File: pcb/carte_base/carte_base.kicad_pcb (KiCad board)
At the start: 2 copper layers, 96 x 53 mm, 40 parts, among them J1 Conn_01x04, J2 Conn_01x02, J3 Conn_01x02, J4 Conn_01x02, SW1 FSMRA3JH04, U1 STM32L031, U2 DAC7563T, U3 TS9222IDT

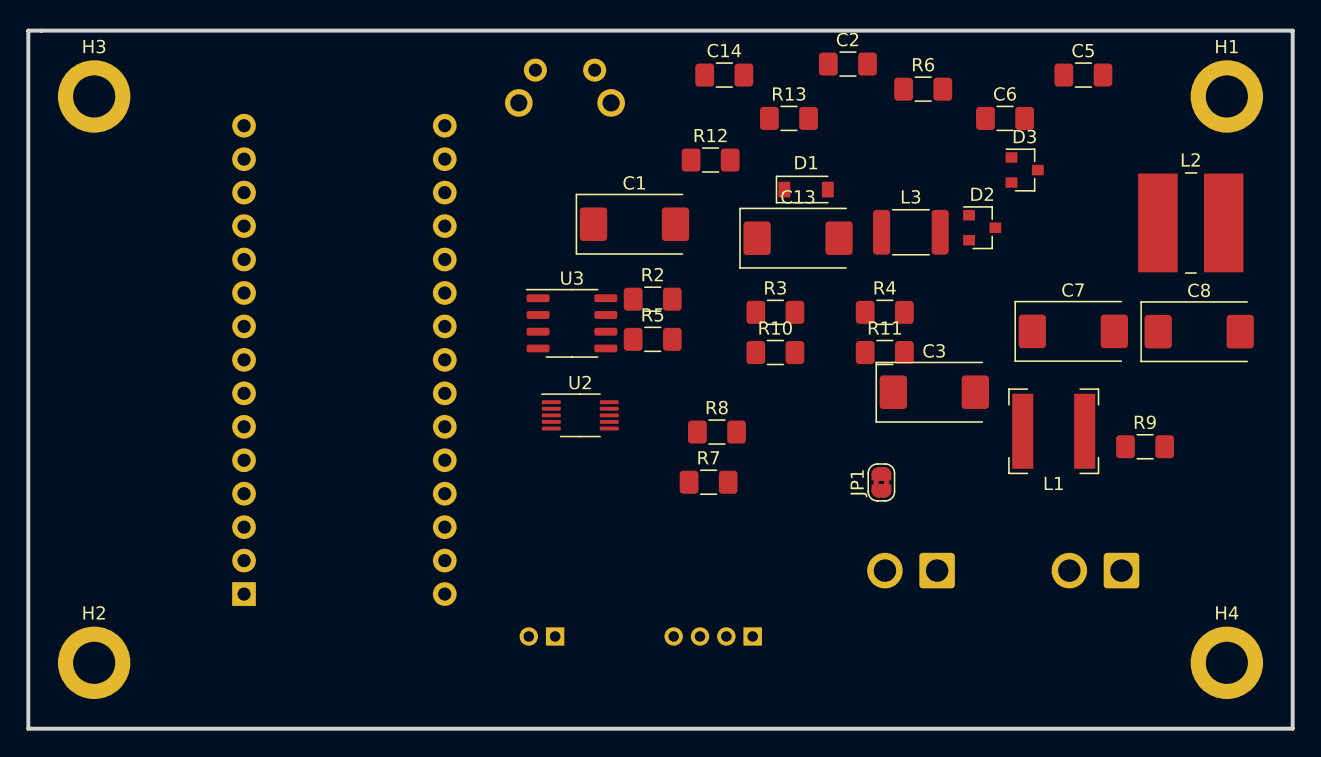
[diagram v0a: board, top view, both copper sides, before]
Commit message: Carte base finie
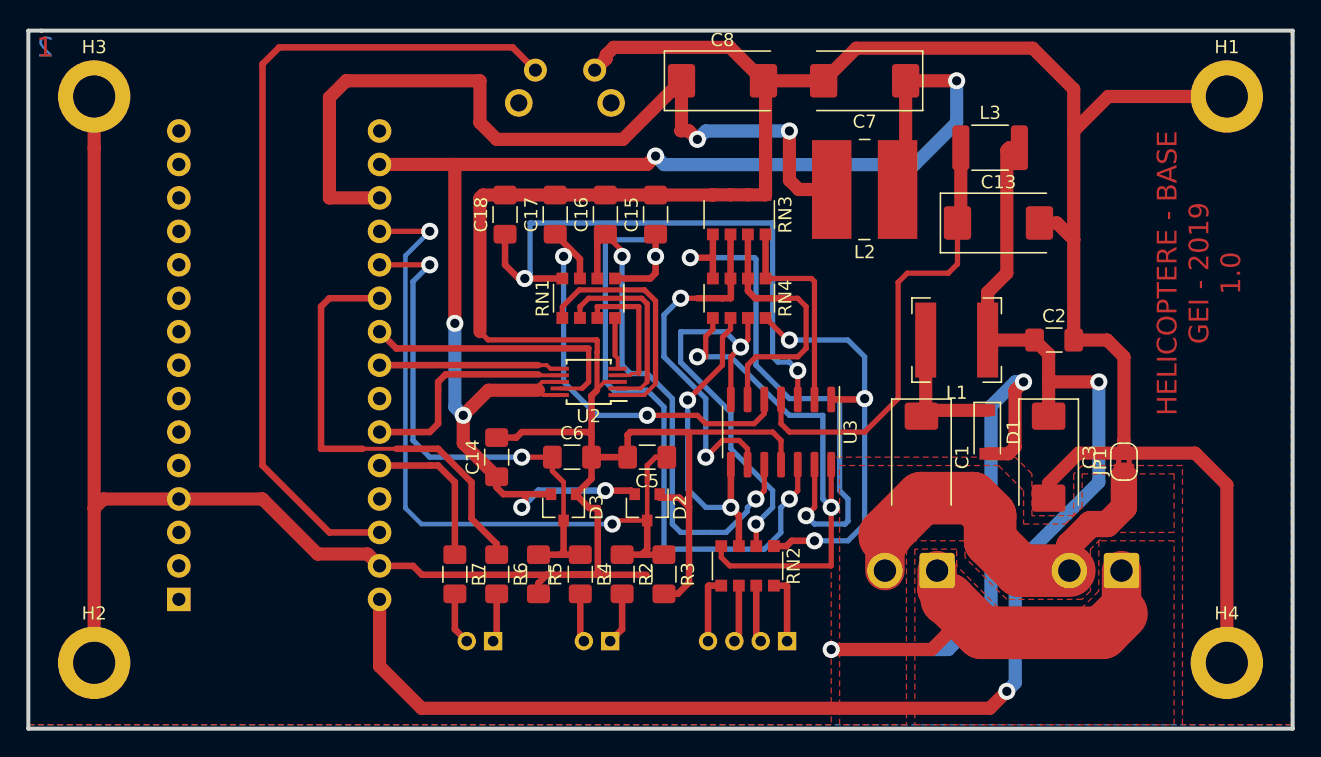
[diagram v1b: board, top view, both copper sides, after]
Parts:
- removed R10, R11, R12, R13, R8, R9: 1K, Resistor_SMD:R_1206_3216Metric_Pad1.42x1.75mm_HandSolder
- added C15: 22nF, Capacitor_SMD:C_1206_3216Metric_Pad1.42x1.75mm_HandSolder, F.Cu at (127.6, 74.0)
- added C16: 22nF, Capacitor_SMD:C_1206_3216Metric_Pad1.42x1.75mm_HandSolder, F.Cu at (123.8, 74.0)
- added C17: 22nF, Capacitor_SMD:C_1206_3216Metric_Pad1.42x1.75mm_HandSolder, F.Cu at (120.0, 74.0)
- added C18: 22nF, Capacitor_SMD:C_1206_3216Metric_Pad1.42x1.75mm_HandSolder, F.Cu at (116.2, 74.0)
- added J5: Conn_01x02, Insa:DF3A-2P-2DS, B.Cu at (123.2, 106.4)
- added RN1: 1K, Resistor_SMD:R_Array_Convex_4x1206, F.Cu at (122.5, 80.3)
- added RN2: 100, Resistor_SMD:R_Array_Convex_4x1206, F.Cu at (134.6, 100.6)
- added RN3: 1K, Resistor_SMD:R_Array_Convex_4x1206, F.Cu at (134.0, 74.0)
- added RN4: 2.4K, Resistor_SMD:R_Array_Convex_4x1206, F.Cu at (134.0, 80.3)
- U2: value DAC7563T -> DAC7554; footprint Package_SO:VSSOP-10_3x3mm_P0.5mm -> Package_SO:MSOP-10_3x3mm_P0.5mm
- U3: value TS9222IDT -> TS9224IDT; footprint Package_SO:SO-8_3.9x4.9mm_P1.27mm -> Package_SO:SOIC-14_3.9x8.7mm_P1.27mm
- moved R6 49.0 mm to (115.6, 101.3), turned to 270 degrees
- moved C5 44.0 mm to (127.0, 92.4), turned to 180 degrees
- moved D3 43.4 mm to (120.6, 96.2), turned to 270 degrees
- moved C6 41.7 mm to (121.3, 92.4)
- moved C8 40.9 mm to (132.7, 63.8)
- moved C14 33.8 mm to (115.6, 92.4), turned to 90 degrees
- moved D2 33.1 mm to (127.0, 96.2), turned to 270 degrees
- moved R4 30.5 mm to (121.9, 101.3), turned to 270 degrees
- moved C1 28.1 mm to (147.8, 92.4), turned to 270 degrees
- moved C2 26.2 mm to (157.9, 83.5)
- moved L2 24.9 mm to (143.5, 72.1), turned to 180 degrees
- moved C7 24.8 mm to (143.5, 63.8), turned to 180 degrees
- moved D1 23.0 mm to (152.8, 90.5), turned to 270 degrees
- moved R3 21.6 mm to (128.3, 101.3), turned to 270 degrees
- moved R2 21.0 mm to (125.1, 101.3), turned to 270 degrees
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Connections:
- C13 pad 1: Net-(C13-Pad1) -> Vdrive
- J1 pad 1: /Consigne_12V_Avant -> /10V_Rotation_VA
- J1 pad 2: /Consigne_12V_Arriere -> /10V_Inclinaison_VA
- J1 pad 3: /Analog_12V_Rotation -> /10V_Rotation_Pos
- J1 pad 4: /Analog_12V_Inclinaison -> /10V_Inclinaison_Pos
- L3 pad 1: Net-(C13-Pad1) -> Vdrive
- R2 pad 2: /Consigne_12V_Avant -> /Consigne_10V_Avant
- R4 pad 2: /Consigne_12V_Arriere -> /Consigne_10V_Arriere
- U1 pad 12: /~DAC_CLEAR -> (no net)
- U2 pad 1: Net-(U2-Pad1) -> Net-(RN1-Pad1)
- U2 pad 10: (no net) -> +3V3
- U2 pad 2: Net-(R13-Pad1) -> Net-(RN1-Pad2)
- U2 pad 4: GND -> Net-(RN1-Pad3)
- U2 pad 5: /~DAC_CLEAR -> Net-(RN1-Pad4)
- U2 pad 6: /~DAC_SYNC -> /DAC_CLK
- U2 pad 7: /DAC_CLK -> /DAC_DATA
- U2 pad 8: /DAC_DATA -> +3V3
- U2 pad 9: +3V3 -> /~DAC_SYNC
- U3 pad 3: Net-(U2-Pad1) -> Net-(C18-Pad1)
- U3 pad 4: GND -> Vdrive
- U3 pad 5: Net-(R13-Pad1) -> Net-(C17-Pad1)
- U3 pad 8: Net-(C13-Pad1) -> Net-(RN2-Pad3)
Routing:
- net GND: track 0.00 -> 322.8 mm
- net +3V3: track 0.00 -> 112.1 mm, vias 0 -> 6
- net VDD: track 0.00 -> 110.6 mm, vias 0 -> 2
- net /Alim_12V: track 0.00 -> 72.1 mm, vias 0 -> 2
- net Net-(C8-Pad1): track 0.00 -> 64.1 mm, vias 0 -> 2
- net Net-(SW1-Pad2): track 0.00 -> 63.4 mm
- net /Consigne_3V3_Avant: track 0.00 -> 56.2 mm, vias 0 -> 2
- net Net-(C15-Pad1): track 0.00 -> 55.1 mm, vias 0 -> 2
- net Net-(C18-Pad1): track 0.00 -> 44.6 mm, vias 0 -> 2
- net Net-(RN3-Pad5): track 0.00 -> 42.8 mm, vias 0 -> 2
- net /Consigne_3V3_Arriere: track 0.00 -> 39.8 mm, vias 0 -> 2
- net Net-(RN2-Pad4): track 0.00 -> 39.6 mm, vias 0 -> 2
- net Net-(C16-Pad1): track 0.00 -> 39.2 mm, vias 0 -> 2
- net Vdrive: track 0.00 -> 34.9 mm
- net /USART_TX: track 0.00 -> 34.3 mm
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- added copper zone on F.Cu, net /Alim_12V
- added copper zone on F.Cu, net /Alim_GND
- added copper zone on B.Cu, net GND
- added copper zone on F.Cu, net GND
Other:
- board text added: "1"
- board text added: "2"
- board text added: "HELICOPTERE - BASE GEI - 2019 1.0"

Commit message: Correction sur carte base
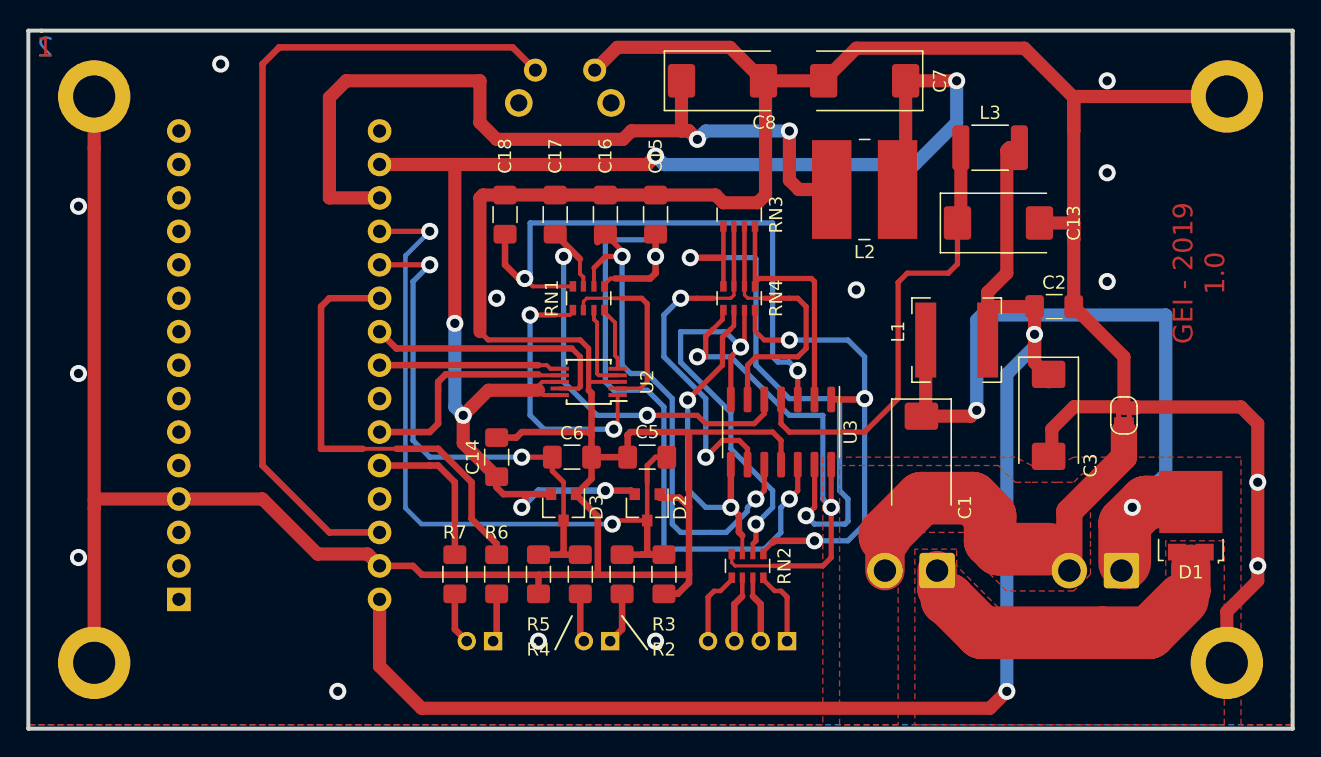
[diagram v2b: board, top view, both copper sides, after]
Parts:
- D1: value D -> D_Schottky_AAK; footprint Diode_SMD:D_SOD-123 -> Package_TO_SOT_SMD:TO-277A
- RN1, RN2, RN3, RN4: footprint Resistor_SMD:R_Array_Convex_4x1206 -> Resistor_SMD:R_Array_Convex_4x0603
- moved D1 16.7 mm to (168.3, 96.8), turned to 180 degrees
- moved JP1 3.52 mm to (163.2, 89.2)
- moved C3 3.18 mm to (157.5, 89.2)
- moved C2 2.54 mm to (157.9, 81.0)
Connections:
- D1 pad 1: +12V -> /Alim_12V
- J3 pad 1: /Alim_12V -> +12V
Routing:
- net +12V: track 11.1 -> 56.0 mm, vias 0 -> 2
- net /Alim_12V: track 72.1 -> 28.5 mm, vias 2 -> 0
- net GND: track 322.8 -> 329.8 mm, vias 0 -> 14
- net Net-(RN1-Pad3): track 10.8 -> 6.53 mm
- net Net-(RN2-Pad1): track 31.5 -> 34.7 mm
- net /Alim_GND: track 31.0 -> 33.5 mm
- net Net-(RN1-Pad1): track 18.3 -> 20.7 mm, vias 0 -> 2
- net VDD: track 110.6 -> 113.0 mm
- net Net-(RN3-Pad8): track 16.1 -> 18.1 mm
- net Net-(RN3-Pad5): track 42.8 -> 44.8 mm
- net /~DAC_SYNC: track 21.3 -> 19.9 mm
- net Net-(RN2-Pad3): track 24.6 -> 26.1 mm
- net Net-(RN2-Pad2): track 31.5 -> 32.7 mm
- net /10V_Inclinaison_VA: track 4.36 -> 5.54 mm
- net /10V_Rotation_Pos: track 4.36 -> 5.54 mm
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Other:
- board text added: "GEI - 2019 1.0"
- board text removed: "HELICOPTERE - BASE GEI - 2019 1.0"

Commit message: petites evolutions sur PCB
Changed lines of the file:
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@@
   )
   (setup
-    (last_trace_width 2)
+    (last_trace_width 0.25)
     (user_trace_width 0.25)
     (user_trace_width 0.3)
@@
     (visible_elements FFFFFF7F)
     (pcbplotparams
-      (layerselection 0x01000_ffffffff)
-      (usegerberextensions false)
+      (layerselection 0x010f0_ffffffff)
+      (usegerberextensions true)
       (usegerberattributes false)
       (usegerberadvancedattributes false)
       (creategerberjobfile false)
-      (excludeedgelayer false)
+      (excludeedgelayer true)
       (linewidth 0.100000)
       (plotframeref false)
@@
       (psa4output false)
       (plotreference true)
-      (plotvalue true)
+      (plotvalue false)
       (plotinvisibletext false)
       (padsonsilk false)
       (subtractmaskfromsilk false)
-      (outputformat 4)
+      (outputformat 1)
       (mirror false)
-      (drillshape 2)
+      (drillshape 0)
       (scaleselection 1)
       (outputdirectory "./"))
@@
     (tags "resistor handsolder")
     (attr smd)
-    (fp_text reference R6 (at -3.175 0 180) (layer F.SilkS)
+    (fp_text reference R6 (at -3.81 0 180) (layer F.SilkS)
       (effects (font (size 1 1) (thickness 0.15)))
     )
@@
     (tags "resistor handsolder")
     (attr smd)
-    (fp_text reference R7 (at -3.175 0 180) (layer F.SilkS)
+    (fp_text reference R7 (at -3.81 0 180) (layer F.SilkS)
       (effects (font (size 1 1) (thickness 0.15)))
     )
@@
     (tags "capacitor tantalum")
     (attr smd)
-    (fp_text reference C3 (at 3.81 -3.175 90) (layer F.SilkS)
+    (fp_text reference C3 (at 3.81 -3.81 90) (layer F.SilkS)
       (effects (font (size 1 1) (thickness 0.15)))
     )
@@
     (tags "SOIC SO")
     (attr smd)
-    (fp_text reference U3 (at 0 -5.28 90) (layer F.SilkS)
+    (fp_text reference U3 (at 0 -5.715 90) (layer F.SilkS)
       (effects (font (size 1 1) (thickness 0.15)))
     )
@@
     (tags "TO-277A SOT-1289")
     (attr smd)
-    (fp_text reference D1 (at 0 -4.3 180) (layer F.SilkS)
+    (fp_text reference D1 (at 0 4.445 180) (layer F.SilkS)
       (effects (font (size 1 1) (thickness 0.15)))
     )
@@
     (effects (font (size 1.5 1.5) (thickness 0.3)))
   )
-  (gr_text "GEI - 2019\n1.0" (at 168.9 78.415 90) (layer F.Cu)
+  (gr_text "GEI - 2019\n1.0" (at 170.424 78.542 90) (layer F.SilkS)
     (effects (font (size 1.5 1.5) (thickness 0.3)))
   )
